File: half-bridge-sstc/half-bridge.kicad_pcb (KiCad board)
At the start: 2 copper layers, 96.5 x 98 mm, 75 parts, among them J1 Current Transformer, J10 Conn_01x01, J11 Conn_01x01, J2 AC Input 18-24 V, J3 Barrel_Jack, J4 Gate Drive Transformer, J5 Reactive Power Meter, J6 External Disable Optocoupler, J7 Conn_01x01, J8 Feedback Antenna, J9 Conn_01x01, U1 tc4420, U2 tc4420, U3 LM7815_TO220, U4 LM339, U6 40106, U7 4N28

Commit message: Fixed long dead time problem on half-bridge-sstc
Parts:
- D3, D4: value 1N5818 -> 1N4148
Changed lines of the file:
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@@
   )
   (setup
-    (last_trace_width 0.5)
+    (last_trace_width 0.25)
     (user_trace_width 0.35)
     (user_trace_width 0.5)
@@
       (effects (font (size 1 1) (thickness 0.15)))
     )
-    (fp_text value 1N5818 (at 3.81 2.41 180) (layer F.Fab)
+    (fp_text value 1N4148 (at 3.81 2.41 180) (layer F.Fab)
       (effects (font (size 1 1) (thickness 0.15)))
     )
@@
       (effects (font (size 1 1) (thickness 0.15)))
     )
-    (fp_text value 1N5818 (at 3.81 2.41 180) (layer F.Fab)
+    (fp_text value 1N4148 (at 3.81 2.41 180) (layer F.Fab)
       (effects (font (size 1 1) (thickness 0.15)))
     )

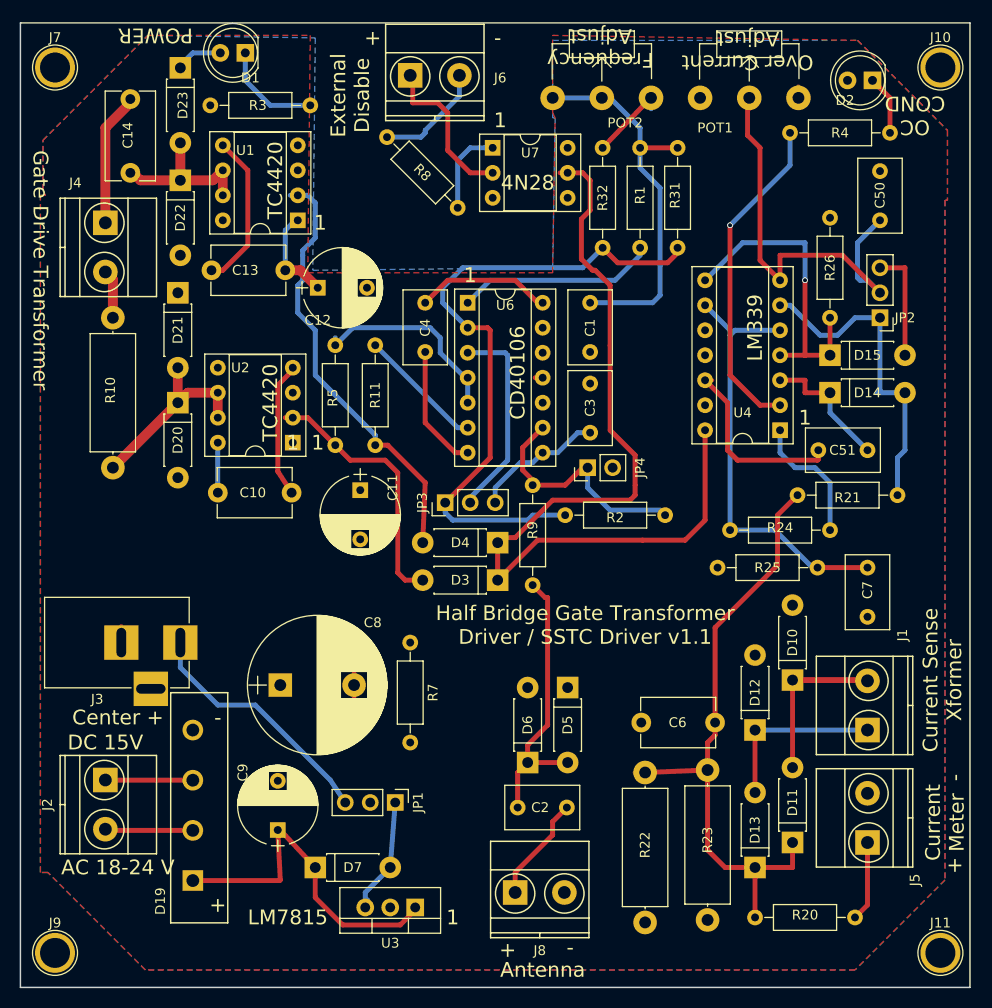
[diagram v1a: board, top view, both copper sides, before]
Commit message: Cleaned up labels and pads on half/full bridge boards
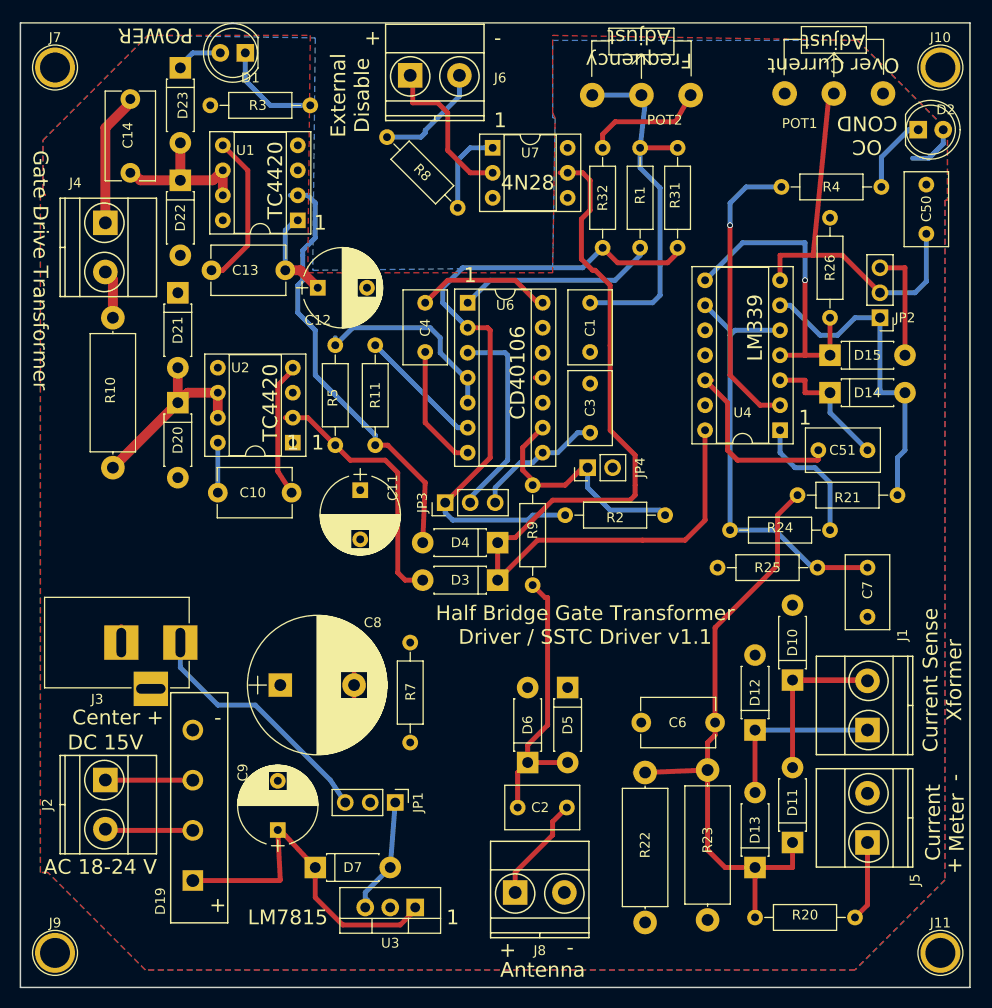
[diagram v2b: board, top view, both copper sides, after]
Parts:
- moved POT1 8.61 mm to (124.2, 52.6)
- moved D2 6.84 mm to (137.7, 56.3), turned to 0 degrees
- moved R4 5.57 mm to (134.0, 62.1)
- moved C50 4.91 mm to (138.6, 66.9)
- moved POT2 4.04 mm to (104.6, 52.8)
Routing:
- net +15V: track 48.6 -> 53.8 mm
- net Net-(C50-Pad1): track 45.3 -> 41.2 mm
- net Net-(R4-Pad2): track 33.5 -> 29.7 mm
- net Net-(POT2-Pad3): track 8.86 -> 12.4 mm
- net Net-(C1-Pad1): track 40.9 -> 39.1 mm
- net Net-(D2-Pad1): track 6.58 -> 7.93 mm
- net GND: track 81.8 -> 80.7 mm

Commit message: Added optional frequency halving to ensure 50% duty cycle
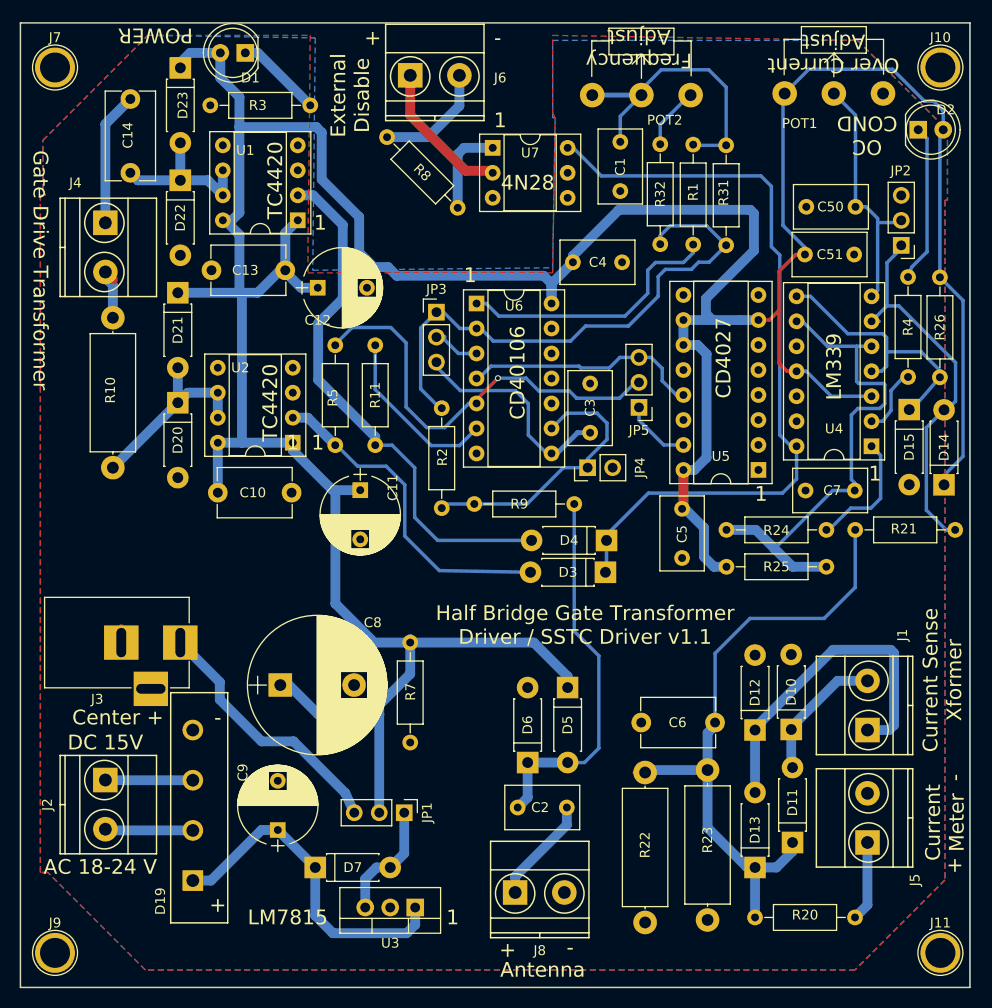
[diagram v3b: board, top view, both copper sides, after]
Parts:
- added C5: 0.1 uF, Capacitors_THT:C_Disc_D7.5mm_W4.4mm_P5.00mm, F.Cu at (113.7, 94.9)
- added JP5: Jumper_NC_Dual, Pin_Headers:Pin_Header_Straight_1x03_Pitch2.54mm, F.Cu at (109.4, 84.5)
- added U5: 4027, Housings_DIP:DIP-16_W7.62mm_Socket, F.Cu at (121.5, 90.9)
- R11, R5: value 10k -> 4k7
- moved R2 22.7 mm to (89.3, 94.8), turned to 90 degrees
- moved C51 20.9 mm to (126.2, 69.0), turned to 0 degrees
- moved JP3 19.4 mm to (88.8, 74.9), turned to 0 degrees
- moved C1 16.6 mm to (107.5, 57.6)
- moved C4 15.6 mm to (102.6, 69.8), turned to 0 degrees
- moved D14 14.9 mm to (140.4, 92.4), turned to 90 degrees
- moved R26 12.7 mm to (139.9, 71.3)
- moved D4 11.1 mm to (106.1, 98.1)
- moved D3 11.0 mm to (106.0, 101.3)
- moved D15 9.77 mm to (136.8, 84.8), turned to 270 degrees
- moved R4 9.55 mm to (136.7, 71.3), turned to 270 degrees
- moved U4 9.44 mm to (133.0, 88.5)
- moved C7 7.94 mm to (131.3, 93.0), turned to 180 degrees
- moved C50 7.70 mm to (131.4, 64.2), turned to 180 degrees
- moved JP2 7.67 mm to (136.0, 68.1)
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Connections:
- R5 pad 2: Net-(R5-Pad2) -> Net-(JP5-Pad2)
- U6 pad 4: Net-(R5-Pad2) -> Net-(JP5-Pad3)
- U6 pad 5: Net-(R5-Pad2) -> Net-(JP5-Pad2)
- U7 pad 5: Net-(D3-Pad1) -> (no net)
- U7 pad 6: (no net) -> Net-(D3-Pad1)
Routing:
- net +15V: track 53.8 -> 390.2 mm
- net GND: track 80.7 -> 2.87 mm
- net Net-(JP5-Pad2): track 0.00 -> 46.0 mm, vias 0 -> 1
- net Net-(JP5-Pad3): track 0.00 -> 24.4 mm
- net Net-(R4-Pad2): track 29.7 -> 7.20 mm, vias 1 -> 0
- net Net-(R5-Pad2): track 22.5 -> 0.00 mm
- net Net-(D12-Pad1): track 17.8 -> 34.4 mm
- net Net-(JP3-Pad2): track 21.2 -> 6.77 mm
- net Net-(C50-Pad1): track 41.2 -> 27.1 mm
- net Net-(JP3-Pad1): track 67.8 -> 56.1 mm
- net Net-(D3-Pad1): track 91.4 -> 80.4 mm
- net Net-(D4-Pad2): track 44.3 -> 54.5 mm
- net Net-(D10-Pad1): track 24.2 -> 14.1 mm
- net Net-(C2-Pad1): track 29.4 -> 39.0 mm
- net Net-(C3-Pad1): track 13.7 -> 23.3 mm
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- added copper zone on B.Cu, net GND
- removed copper zone on B.Cu, net +15V
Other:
- board text added: "CD4027"
